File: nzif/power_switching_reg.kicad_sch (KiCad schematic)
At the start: 33 parts, among them U1101 ADP2303ARDZ, U1102 ADP2303ARDZ, U1103 ADP2303ARDZ

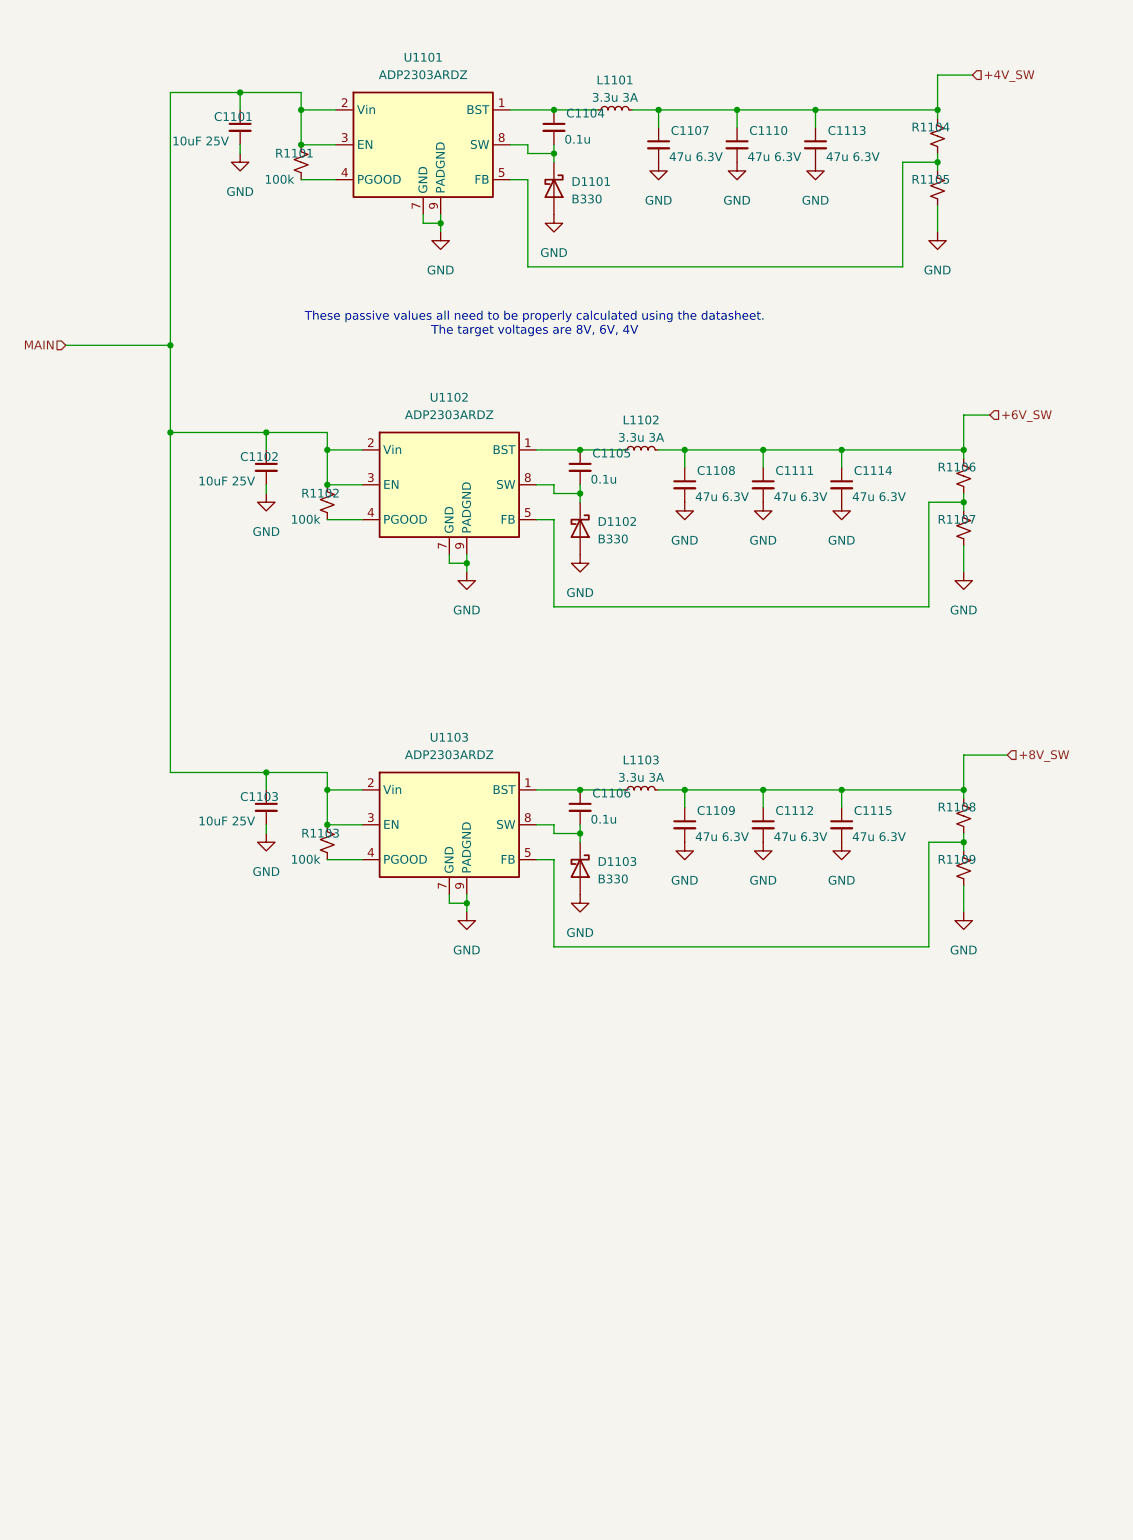
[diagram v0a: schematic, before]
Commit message: added -3.5V rail
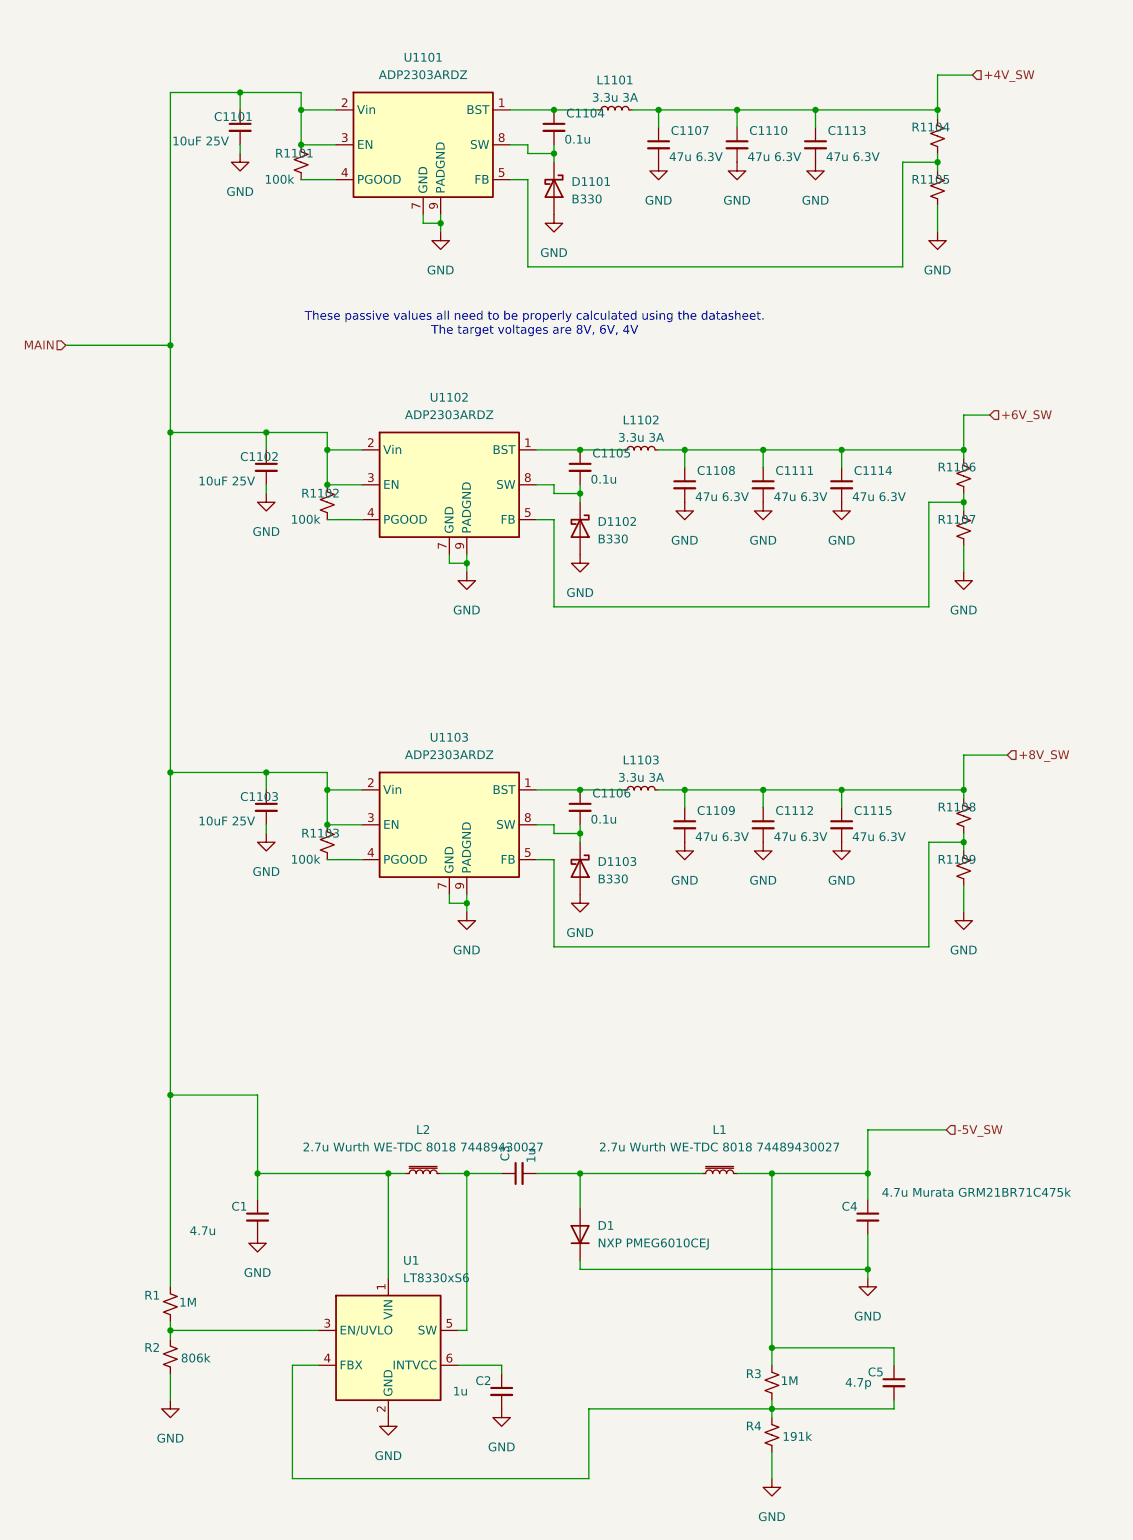
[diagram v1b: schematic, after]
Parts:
- added C1: 4.7u, Capacitor_SMD:C_0603_1608Metric, symbol Device:C_Small
- added C2, C3: 1u, Capacitor_SMD:C_0603_1608Metric, symbol Device:C_Small
- added C4: 4.7u Murata GRM21BR71C475k, Capacitor_SMD:C_0603_1608Metric, symbol Device:C_Small
- added C5: 4.7p, Capacitor_SMD:C_0603_1608Metric, symbol Device:C_Small
- added D1: NXP PMEG6010CEJ, symbol Diode:1N4148WT
- added L1, L2: 2.7u Wurth WE-TDC 8018 74489430027, symbol Device:L_Iron_Small
- added R1, R3: 1M, Resistor_SMD:R_0603_1608Metric, symbol Device:R_Small_US
- added R2: 806k, Resistor_SMD:R_0603_1608Metric, symbol Device:R_Small_US
- added R4: 191k, Resistor_SMD:R_0603_1608Metric, symbol Device:R_Small_US
- added U1: LT8330xS6, Package_TO_SOT_SMD:TSOT-23-6, symbol nzif_radio_symbol_library:LT8330xS6
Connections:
- net GND: now also C1.2, C2.2, C4.2, D1.1 (K), R2.2, R4.2, U1.2 (GND)
- net MAIN: now also C1.1, L2.1, R1.1, U1.1 (VIN)
- new net: C3.2, D1.2 (A), L1.1
- new net: C2.1, U1.6 (INTVCC)
- new net: C5.2, R3.2, R4.1, U1.4 (FBX)
- new net: R1.2, R2.1, U1.3 (EN/UVLO)
- new net: C3.1, L2.2, U1.5 (SW)
- new net -5V_SW: C4.1, C5.1, L1.2, R3.1

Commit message: upgrade to v10
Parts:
- R1104, R1105, R1106, R1107, R1108, R1109: value ~ -> (none)

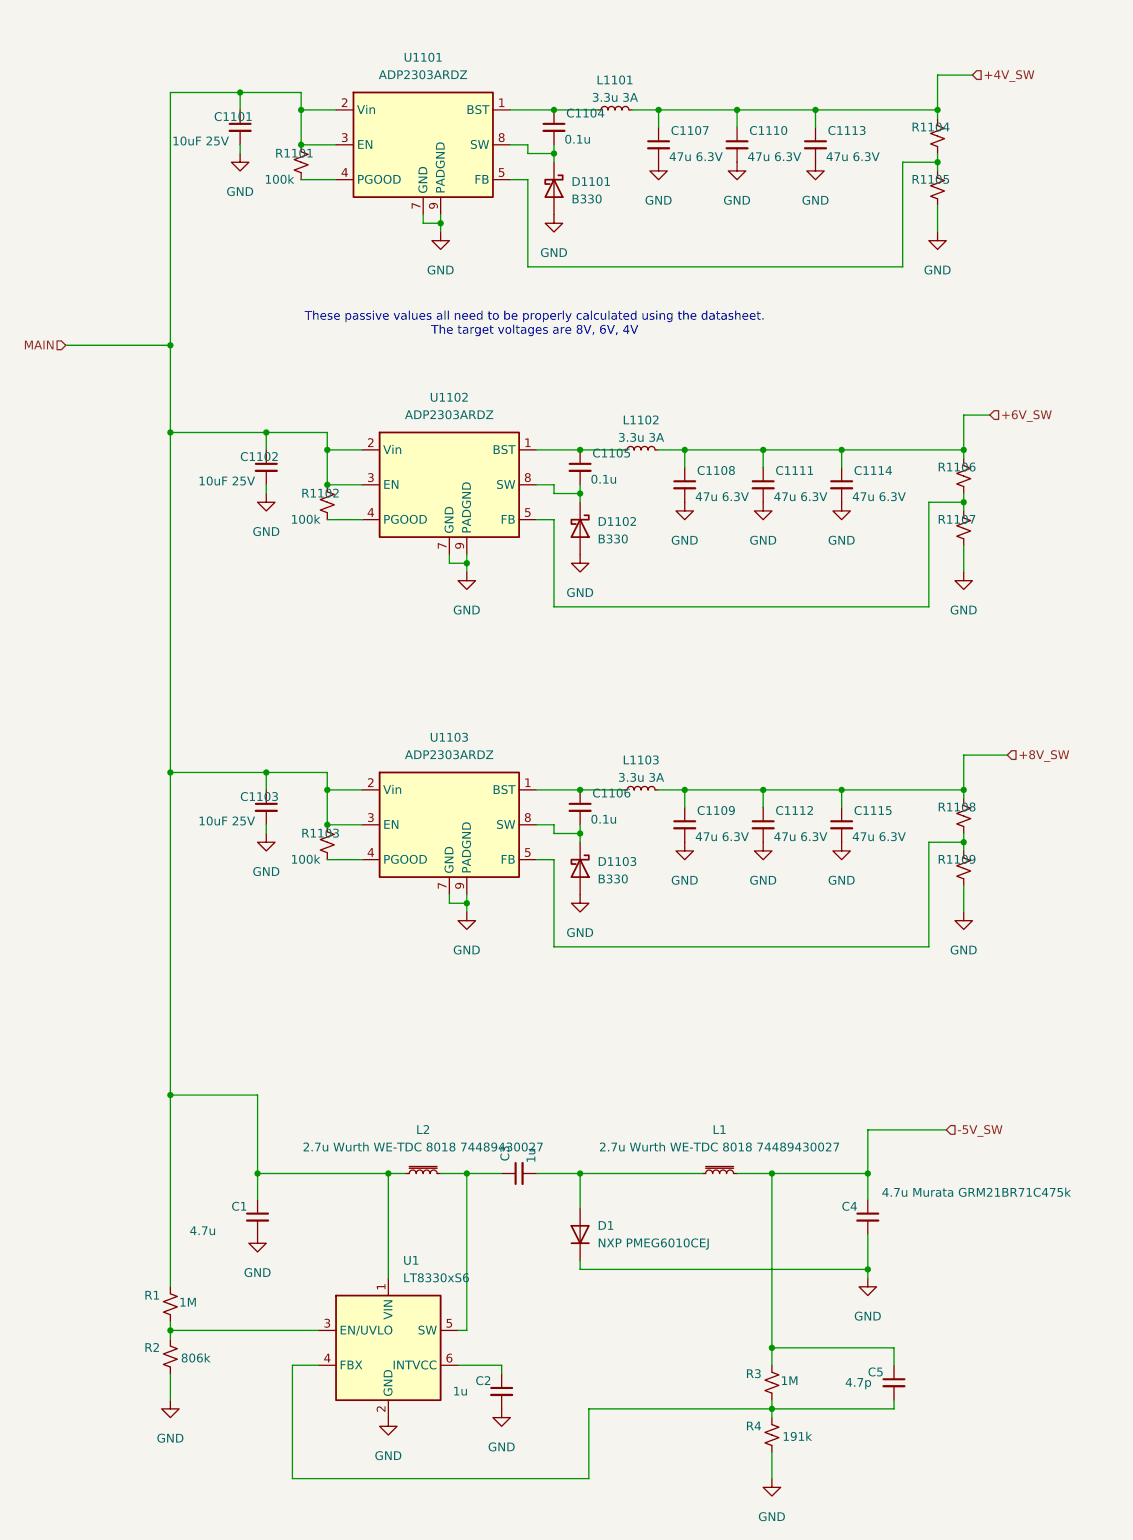
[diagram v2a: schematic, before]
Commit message: top sheet wiring
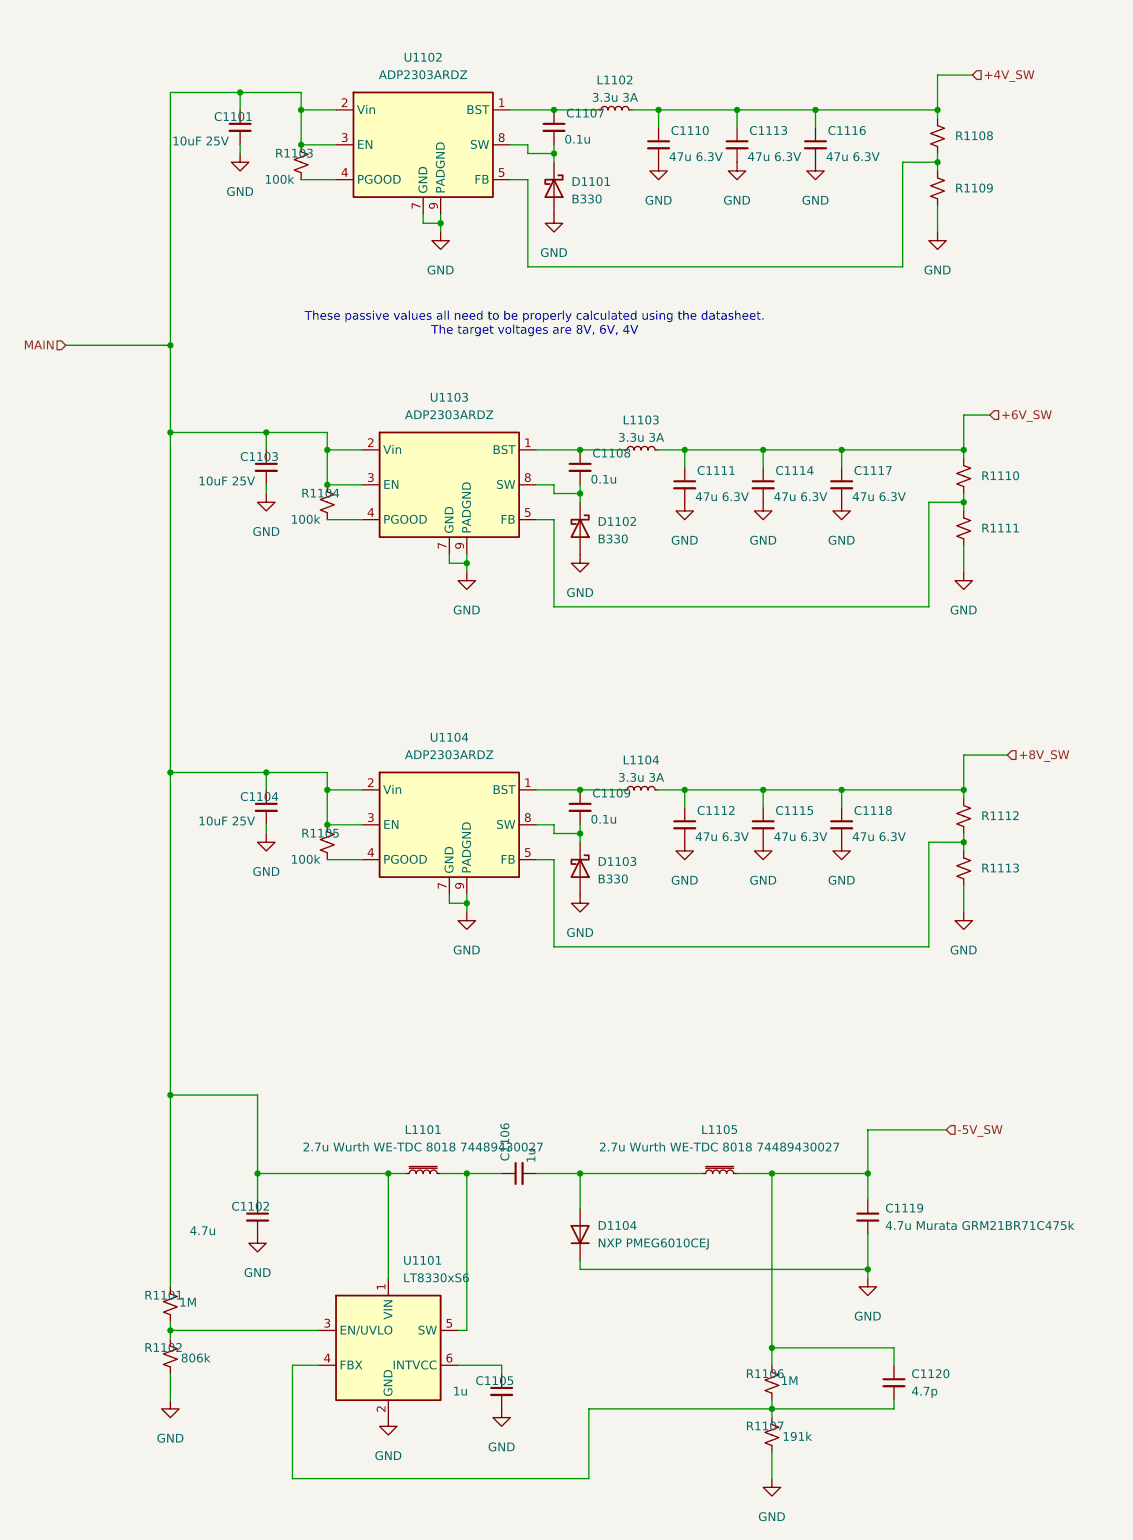
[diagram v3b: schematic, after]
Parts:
- renumbered C1 to C1102, C1102 to C1103, C1103 to C1104, C2 to C1105, C3 to C1106, C1104 to C1107, C1105 to C1108, C1106 to C1109, C1107 to C1110, C1108 to C1111, C1109 to C1112, C1110 to C1113, C1111 to C1114, C1112 to C1115, C1113 to C1116, C1114 to C1117, C1115 to C1118, C4 to C1119, C5 to C1120, D1 to D1104, L2 to L1101, L1101 to L1102, L1102 to L1103, L1103 to L1104, L1 to L1105, R1 to R1101, R2 to R1102, R1101 to R1103, R1102 to R1104, R1103 to R1105, R3 to R1106, R4 to R1107, R1104 to R1108, R1105 to R1109, R1106 to R1110, R1107 to R1111, R1108 to R1112, R1109 to R1113, U1 to U1101, U1101 to U1102, U1102 to U1103, U1103 to U1104

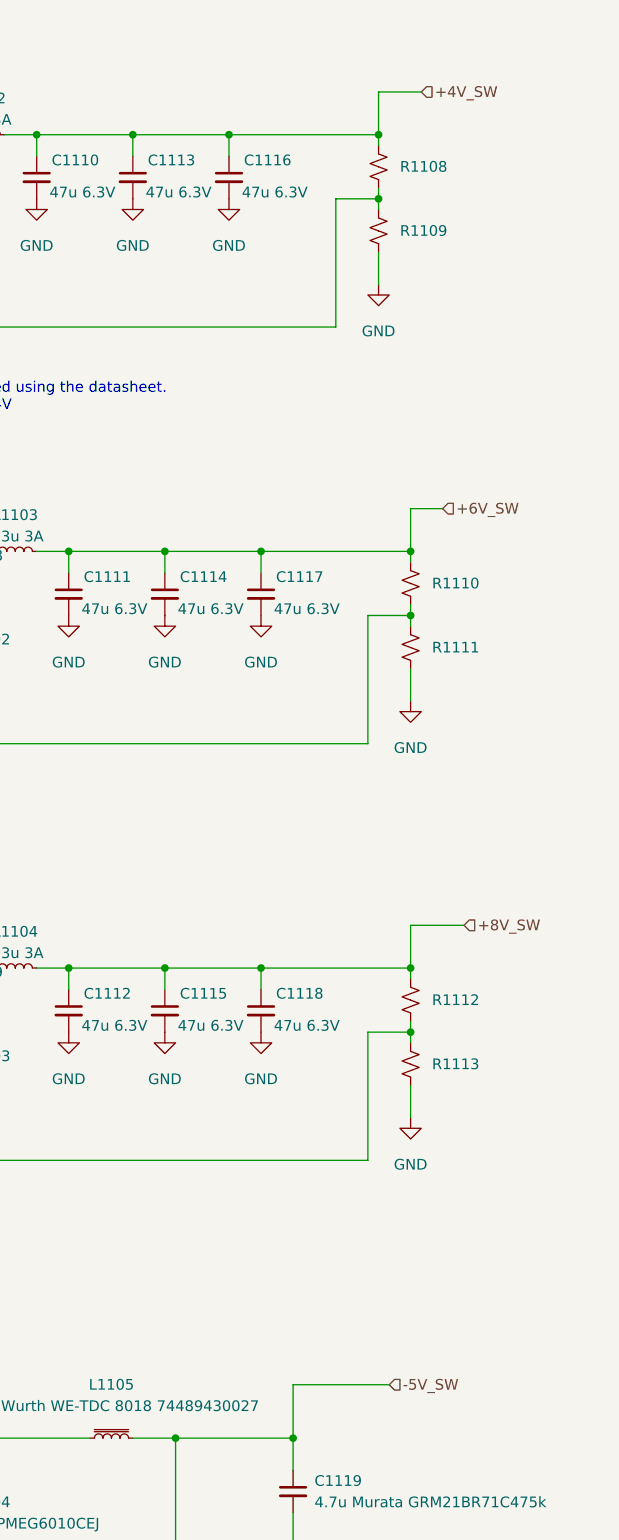
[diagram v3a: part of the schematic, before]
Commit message: corrected some errors from erc report
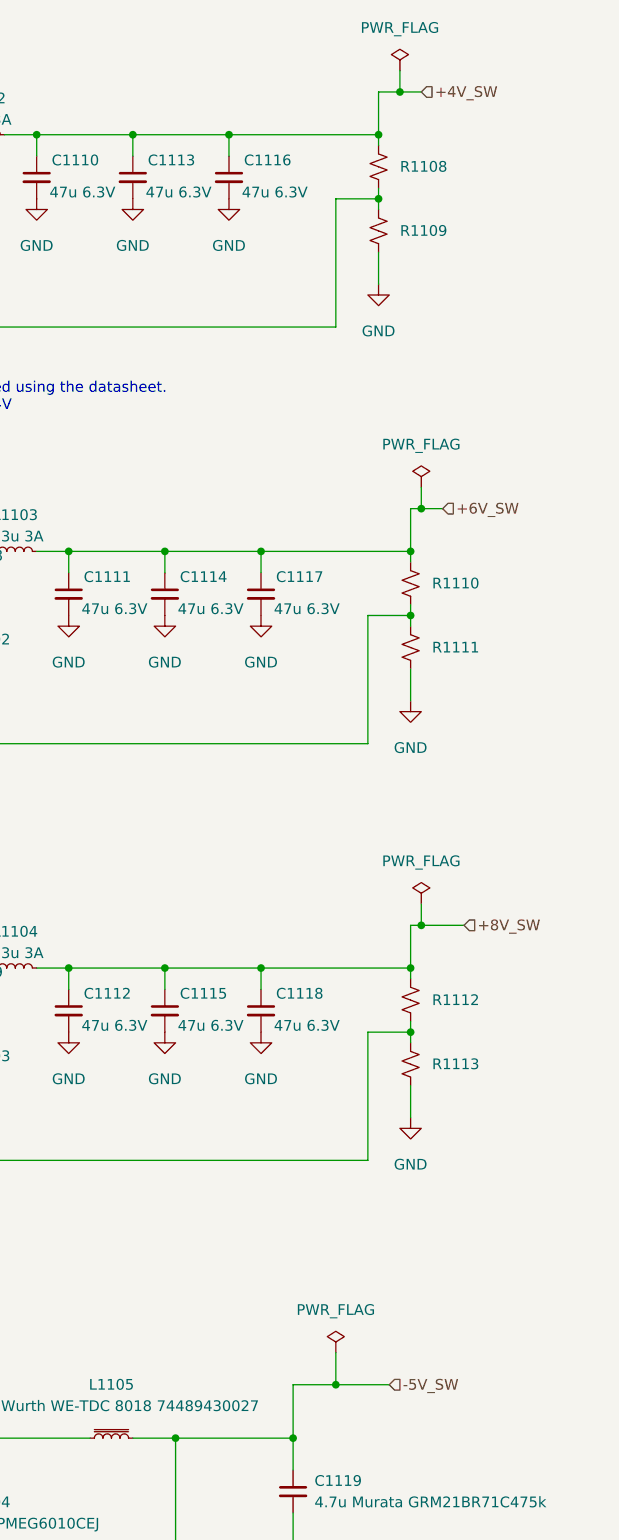
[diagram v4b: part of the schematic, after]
